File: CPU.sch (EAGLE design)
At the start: 13 parts, among them IC1 Z80CPU, IC4 XR-16C550P, IC5 HM62256DIP, J1 DCJ0202

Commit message: Start Splitting into multiple boards
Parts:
- removed D1: 1N4942, diode:1N4942
- removed IC5: HM62256DIP, jean:HM62256DIP
- removed J1: DCJ0202, con-jack:DCJ0202
- removed U$1: AT28C256ZIF, bt_memory:AT28C256ZIF
- added JP1: (no value), jean:JEANNECTOR/90
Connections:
- removed net !IORQ: IC1.IORQ, V2/3.B, V2/4.A
- removed net !MREQ: IC1.MREQ, V2/1.A, V3/3.B
- removed net N$2: U$1.!CE, V3/3.Y
- removed net N$4: V2/1.B, V3/2.Y
- new net N$1: IC1.M1, JP1.!M1
- new net N$10: IC1.WR, JP1.!WR
- new net N$14: IC1.RD, JP1.!RD
- new net N$16: IC1.IORQ, JP1.!IOREQ
- new net N$19: V2/4.A
- new net N$22: IC1.BUSAK, JP1.!BUSACK
- new net N$8: IC1.MREQ, JP1.!MREQ
- net !RD: no longer IC1.RD, IC5.!RE, U$1.!OE
- net !RESET: now also JP1.!RESET
- net !WR: no longer IC1.WR, IC5.!WE
- net A0: now also JP1.A0; no longer IC5.A0, U$1.A0
- net A1: now also JP1.A1; no longer IC5.A1, U$1.A1
- net A10: now also JP1.A10; no longer IC5.A10, U$1.A10
- net A11: now also JP1.A11; no longer IC5.A11, U$1.A11
- net A12: now also JP1.A12; no longer IC5.A12, U$1.A12
- net A13: now also JP1.A13; no longer IC5.A13, U$1.A13
- net A14: now also JP1.A14; no longer IC5.A14, U$1.A14
- net A15: now also JP1.A15; no longer V3/2.A, V3/2.B, V3/3.A
- net A2: now also JP1.A2; no longer IC5.A2, U$1.A2
- net A3: now also JP1.A3; no longer IC5.A3, U$1.A3
- net A4: now also JP1.A4; no longer IC5.A4, U$1.A4
- net A5: now also JP1.A5; no longer IC5.A5, U$1.A5
- net A6: now also JP1.A6; no longer IC5.A6, U$1.A6
- net A7: now also JP1.A7; no longer IC5.A7, U$1.A7, V2/3.A
- net A8: now also JP1.A8; no longer IC5.A8, U$1.A8
- net A9: now also JP1.A9; no longer IC5.A9, U$1.A9
- net CLOCK: now also JP1.CLK
- net D0: now also JP1.D0; no longer IC5.D0, U$1.IO0
- net D1: now also JP1.D1; no longer IC5.D1, U$1.IO1
- net D2: now also JP1.D2; no longer IC5.D2, U$1.IO2
- net D3: now also JP1.D3; no longer IC5.D3, U$1.IO3
- net D4: now also JP1.D4; no longer IC5.D4, U$1.IO4
- net D5: now also JP1.D5; no longer IC5.D5, U$1.IO5
- net D6: now also JP1.D6; no longer IC5.D6, U$1.IO6
- net D7: now also JP1.D7; no longer IC5.D7, U$1.IO7
- net GND: now also JP1.GND@1, JP1.GND@2; no longer D1.A, IC5.GND, J1.3, U$1.GND
- net N$9: now also IC1.HALT, JP1.!HALT; no longer IC5.!CE, V2/1.Y
- net VCC: now also JP1.!BUSRQ, JP1.!INT, JP1.!NMI, JP1.VCC; no longer D1.C, IC5.VCC, J1.1, U$1.VCC
- net WAIT: now also JP1.!WAIT
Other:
- note removed: "0x0000 - 0x7FFF"
- note removed: "0x8000 - 0xFFFF"

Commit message: Move away Serial CF
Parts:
- removed IC4: XR-16C550P, exar:XR-16C550P
- removed R1: 1k, eagle-ltspice:R0207/10
- removed S1: RESET, switch-omron:10-XX
- removed SV1: SERIAL, con-lstb:MA04-1
- removed SV2: IDE PATA, con-lstb:MA20-2
- removed V2, V3: 74HC00N, 74ttl-din:74HC00N
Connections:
- removed net !RD: IC4G$1.IOR~, SV2.25
- removed net !WR: IC4G$1.IOW~, SV2.23
- removed net IOCS1: SV2.37, V2/4.Y
- removed net N$11: IC4G$1.TX, SV1.1
- removed net N$13: IC4G$1.BAUDOUT~, IC4G$1.RCLK
- removed net N$15: IC4G$1.RX, SV1.2
- removed net N$17: V2/4.B, V3/1.Y
- removed net N$18: IC4G$1.CS2~, V2/3.Y
- removed net N$19: V2/4.A
- removed net N$20: R1.1, SV2.38
- removed net RESET: IC4G$1.RESET, V2/2.Y
- net !RESET: no longer S1.S, S1.S1, SV2.1, V2/2.A, V2/2.B
- net A0: no longer IC4G$1.A0, SV2.35
- net A1: no longer IC4G$1.A1, SV2.33
- net A2: no longer IC4G$1.A2, SV2.36
- net A7: no longer V3/1.A, V3/1.B
- net CLOCK: no longer IC4G$1.XTAL1
- net D0: no longer IC4G$1.D0, SV2.17
- net D1: no longer IC4G$1.D1, SV2.15
- net D2: no longer IC4G$1.D2, SV2.13
- net D3: no longer IC4G$1.D3, SV2.11
- net D4: no longer IC4G$1.D4, SV2.9
- net D5: no longer IC4G$1.D5, SV2.7
- net D6: no longer IC4G$1.D6, SV2.5
- net D7: no longer IC4G$1.D7, SV2.3
- net GND: no longer IC4G$1.AS~, IC4G$1.IOR, IC4G$1.IOW, S1.P, SV1.4, SV2.19, SV2.2, SV2.22, SV2.24, SV2.26, SV2.30, SV2.40, V2/-UB.-UB, V3/-UB.-UB
- net VCC: no longer IC4G$1.CD~, IC4G$1.CS0, IC4G$1.CS1, IC4G$1.DSR~, IC4G$1.RI~, R1.2, SV1.3, SV2.20, V2/+UB.+UB, V3/+UB.+UB
- net WAIT: no longer SV2.27
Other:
- note removed: "A7 = 0"
- note removed: "A7 = 1"

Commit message: Finish Modularization
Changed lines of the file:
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@@
 <wire x1="96.52" y1="20.32" x2="104.14" y2="20.32" width="0.1524" layer="91"/>
 <wire x1="104.14" y1="20.32" x2="104.14" y2="5.08" width="0.1524" layer="91"/>
-<wire x1="104.14" y1="5.08" x2="-10.16" y2="5.08" width="0.1524" layer="91"/>
-<wire x1="-10.16" y1="5.08" x2="-10.16" y2="43.18" width="0.1524" layer="91"/>
+<wire x1="104.14" y1="5.08" x2="-11.684" y2="5.08" width="0.1524" layer="91"/>
+<wire x1="-11.684" y1="5.08" x2="-11.684" y2="43.18" width="0.1524" layer="91"/>
 <pinref part="IC1" gate="1" pin="BUSAK"/>
-<wire x1="-10.16" y1="43.18" x2="-5.08" y2="43.18" width="0.1524" layer="91"/>
+<wire x1="-11.684" y1="43.18" x2="-5.08" y2="43.18" width="0.1524" layer="91"/>
 </segment>
 </net>
@@
 </sheet>
 </sheets>
-<errors>
-</errors>
 </schematic>
 </drawing>

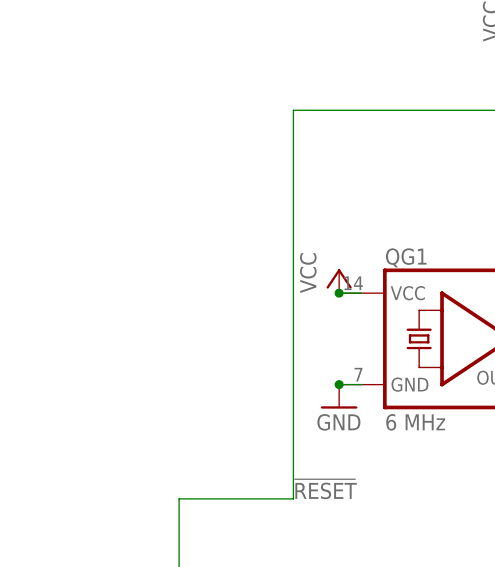
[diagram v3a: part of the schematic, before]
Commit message: Add Decoupling Capacitors.
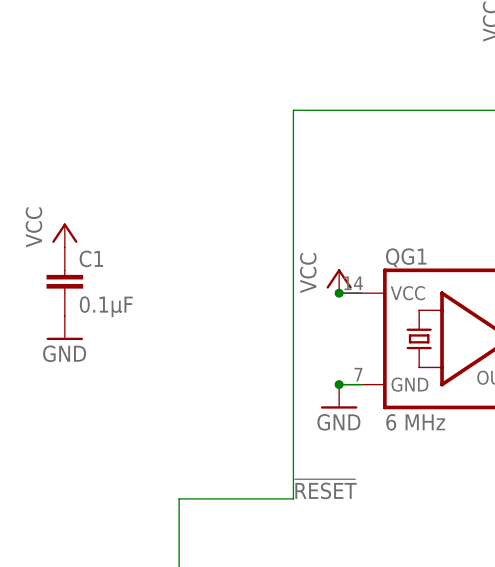
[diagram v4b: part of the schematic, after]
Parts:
- added C1: 0.1µF, capacitor-wima:C5/2.5
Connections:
- net GND: now also C1.2
- net VCC: now also C1.1
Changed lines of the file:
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@@
 <part name="GND1" library="supply1" deviceset="GND" device=""/>
 <part name="GND2" library="supply1" deviceset="GND" device=""/>
+<part name="C1" library="capacitor-wima" deviceset="C" device="5/2.5" value="0.1µF"/>
+<part name="P+1" library="supply1" deviceset="VCC" device=""/>
+<part name="GND3" library="supply1" deviceset="GND" device=""/>
 </parts>
 <sheets>
@@
 <instance part="GND1" gate="1" x="137.16" y="48.26"/>
 <instance part="GND2" gate="1" x="127" y="15.24"/>
+<instance part="C1" gate="G$1" x="-83.82" y="45.72"/>
+<instance part="P+1" gate="VCC" x="-83.82" y="50.8"/>
+<instance part="GND3" gate="1" x="-83.82" y="38.1"/>
 </instances>
 <busses>
@@
 <wire x1="96.52" y1="53.34" x2="137.16" y2="53.34" width="0.1524" layer="91"/>
 </segment>
+<segment>
+<pinref part="C1" gate="G$1" pin="1"/>
+<pinref part="P+1" gate="VCC" pin="VCC"/>
+</segment>
 </net>
 <net name="GND" class="0">
@@
 <wire x1="129.54" y1="55.88" x2="96.52" y2="55.88" width="0.1524" layer="91"/>
 </segment>
-</net>
+<segment>
+<pinref part="C1" gate="G$1" pin="2"/>
+<pinref part="GND3" gate="1" pin="GND"/>
+</segment>
+</net>

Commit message: Add PullUp to reset of cpu
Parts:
- added R1: 3.3k, resistor:R-EU_0207/2V
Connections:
- net !RESET: now also R1.1
- net VCC: now also R1.2
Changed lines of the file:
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@@
 <part name="P+1" library="supply1" deviceset="VCC" device=""/>
 <part name="GND3" library="supply1" deviceset="GND" device=""/>
+<part name="R1" library="resistor" deviceset="R-EU_" device="0207/2V" value="3.3k"/>
+<part name="P+3" library="supply1" deviceset="VCC" device=""/>
 </parts>
 <sheets>
@@
 <instance part="P+1" gate="VCC" x="-83.82" y="50.8"/>
 <instance part="GND3" gate="1" x="-83.82" y="38.1"/>
+<instance part="R1" gate="G$1" x="-53.34" y="68.58" rot="R90"/>
+<instance part="P+3" gate="VCC" x="-53.34" y="76.2"/>
 </instances>
 <busses>
@@
 <pinref part="P+1" gate="VCC" pin="VCC"/>
 </segment>
+<segment>
+<pinref part="R1" gate="G$1" pin="2"/>
+<pinref part="P+3" gate="VCC" pin="VCC"/>
+</segment>
 </net>
 <net name="GND" class="0">
@@
 <wire x1="-71.12" y1="-20.32" x2="-71.12" y2="20.32" width="0.1524" layer="91"/>
 <wire x1="-71.12" y1="20.32" x2="-58.42" y2="20.32" width="0.1524" layer="91"/>
-<wire x1="-10.16" y1="63.5" x2="-58.42" y2="63.5" width="0.1524" layer="91"/>
-</segment>
-</net>
+<wire x1="-10.16" y1="63.5" x2="-53.34" y2="63.5" width="0.1524" layer="91"/>
+<pinref part="R1" gate="G$1" pin="1"/>
+<wire x1="-53.34" y1="63.5" x2="-58.42" y2="63.5" width="0.1524" layer="91"/>
+<junction x="-53.34" y="63.5"/>
+</segment>
+</net>

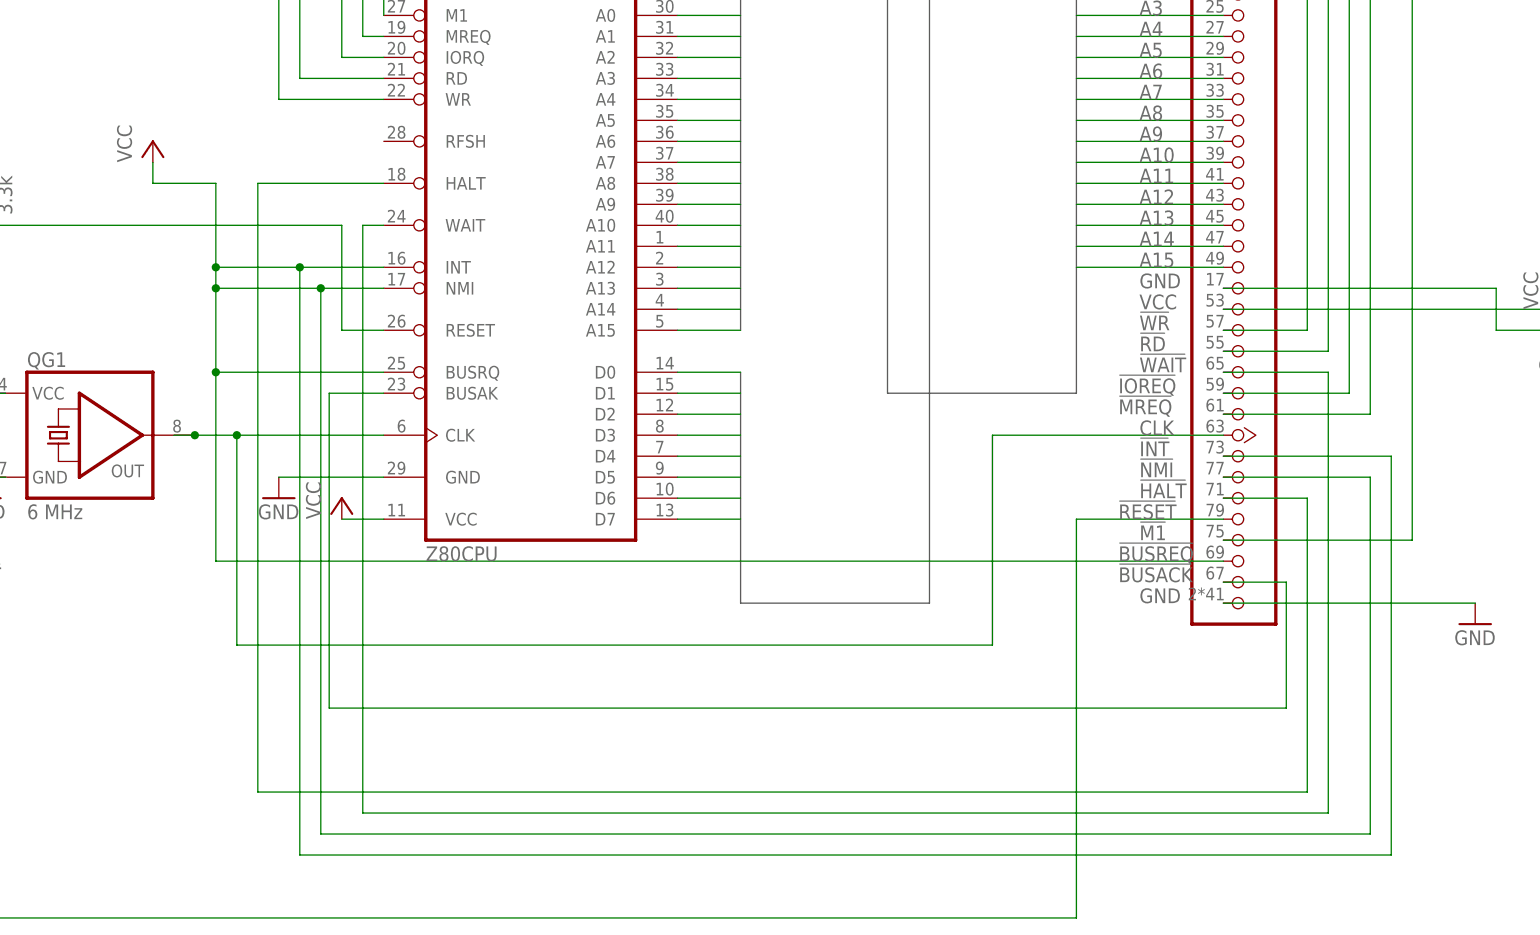
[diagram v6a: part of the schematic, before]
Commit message: Add PullUps to CPU Board
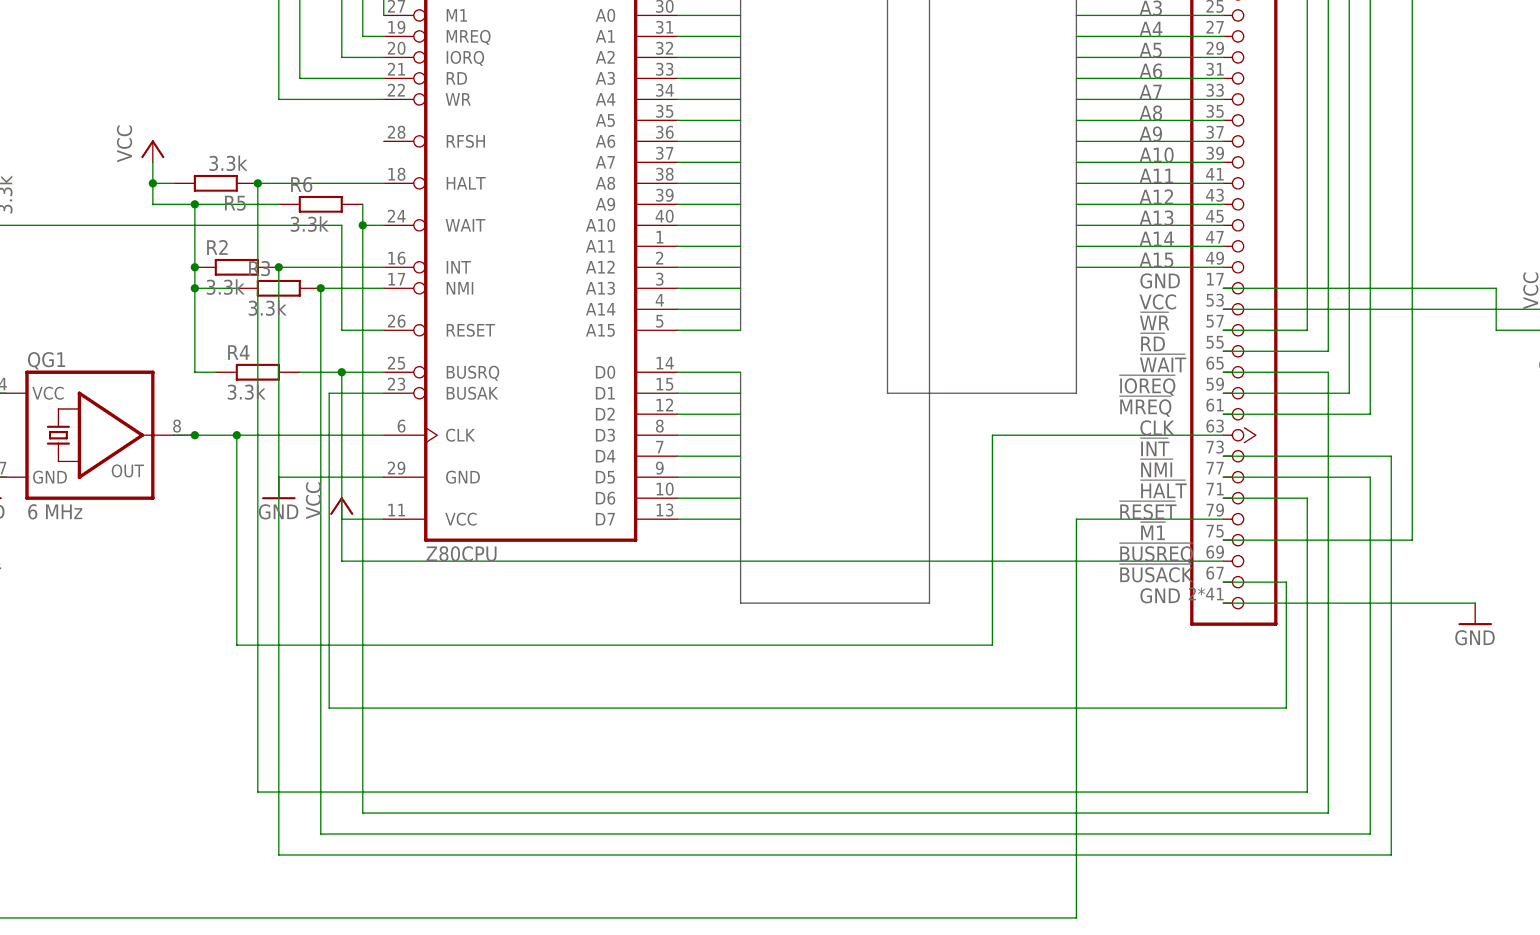
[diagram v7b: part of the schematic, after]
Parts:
- added R2, R3, R4, R5, R6: 3.3k, resistor:R-EU_0207/2V
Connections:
- new net N$2: IC1.BUSRQ, JP1.!BUSRQ, R4.2
- new net N$3: IC1.NMI, JP1.!NMI, R3.2
- new net N$4: IC1.INT, JP1.!INT, R2.2
- net N$9: now also R5.1
- net VCC: now also R2.1, R3.1, R4.1, R5.2, R6.1; no longer IC1.BUSRQ, IC1.INT, IC1.NMI, JP1.!BUSRQ, JP1.!INT, JP1.!NMI
- net WAIT: now also R6.2
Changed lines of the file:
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@@
 <part name="R1" library="resistor" deviceset="R-EU_" device="0207/2V" value="3.3k"/>
 <part name="P+3" library="supply1" deviceset="VCC" device=""/>
+<part name="R2" library="resistor" deviceset="R-EU_" device="0207/2V" value="3.3k"/>
+<part name="R3" library="resistor" deviceset="R-EU_" device="0207/2V" value="3.3k"/>
+<part name="R4" library="resistor" deviceset="R-EU_" device="0207/2V" value="3.3k"/>
+<part name="R5" library="resistor" deviceset="R-EU_" device="0207/2V" value="3.3k"/>
+<part name="R6" library="resistor" deviceset="R-EU_" device="0207/2V" value="3.3k"/>
 </parts>
 <sheets>
@@
 <instance part="R1" gate="G$1" x="-53.34" y="68.58" rot="R90"/>
 <instance part="P+3" gate="VCC" x="-53.34" y="76.2"/>
+<instance part="R2" gate="G$1" x="-22.86" y="58.42"/>
+<instance part="R3" gate="G$1" x="-17.78" y="55.88"/>
+<instance part="R4" gate="G$1" x="-20.32" y="45.72"/>
+<instance part="R5" gate="G$1" x="-25.4" y="68.58" rot="R180"/>
+<instance part="R6" gate="G$1" x="-12.7" y="66.04"/>
 </instances>
 <busses>
@@
 <pinref part="P+10" gate="VCC" pin="VCC"/>
 <wire x1="-33.02" y1="71.12" x2="-33.02" y2="68.58" width="0.1524" layer="91"/>
-<pinref part="IC1" gate="1" pin="BUSRQ"/>
-<wire x1="-5.08" y1="45.72" x2="-25.4" y2="45.72" width="0.1524" layer="91"/>
-<wire x1="-25.4" y1="45.72" x2="-25.4" y2="55.88" width="0.1524" layer="91"/>
-<wire x1="-25.4" y1="55.88" x2="-25.4" y2="58.42" width="0.1524" layer="91"/>
-<wire x1="-25.4" y1="58.42" x2="-25.4" y2="68.58" width="0.1524" layer="91"/>
-<pinref part="IC1" gate="1" pin="INT"/>
-<wire x1="-5.08" y1="58.42" x2="-15.24" y2="58.42" width="0.1524" layer="91"/>
-<junction x="-25.4" y="58.42"/>
-<pinref part="IC1" gate="1" pin="NMI"/>
-<wire x1="-15.24" y1="58.42" x2="-25.4" y2="58.42" width="0.1524" layer="91"/>
-<wire x1="-5.08" y1="55.88" x2="-12.7" y2="55.88" width="0.1524" layer="91"/>
-<junction x="-25.4" y="55.88"/>
-<wire x1="-12.7" y1="55.88" x2="-25.4" y2="55.88" width="0.1524" layer="91"/>
-<wire x1="-33.02" y1="68.58" x2="-25.4" y2="68.58" width="0.1524" layer="91"/>
-<pinref part="JP1" gate="A" pin="!INT"/>
-<wire x1="96.52" y1="35.56" x2="116.84" y2="35.56" width="0.1524" layer="91"/>
-<wire x1="116.84" y1="35.56" x2="116.84" y2="-12.7" width="0.1524" layer="91"/>
-<wire x1="116.84" y1="-12.7" x2="-15.24" y2="-12.7" width="0.1524" layer="91"/>
-<wire x1="-15.24" y1="-12.7" x2="-15.24" y2="58.42" width="0.1524" layer="91"/>
-<junction x="-15.24" y="58.42"/>
-<wire x1="-12.7" y1="55.88" x2="-12.7" y2="-10.16" width="0.1524" layer="91"/>
-<junction x="-12.7" y="55.88"/>
-<wire x1="-12.7" y1="-10.16" x2="114.3" y2="-10.16" width="0.1524" layer="91"/>
-<wire x1="114.3" y1="-10.16" x2="114.3" y2="33.02" width="0.1524" layer="91"/>
-<pinref part="JP1" gate="A" pin="!NMI"/>
-<wire x1="114.3" y1="33.02" x2="96.52" y2="33.02" width="0.1524" layer="91"/>
-<pinref part="JP1" gate="A" pin="!BUSRQ"/>
-<wire x1="96.52" y1="22.86" x2="-25.4" y2="22.86" width="0.1524" layer="91"/>
-<wire x1="-25.4" y1="22.86" x2="-25.4" y2="45.72" width="0.1524" layer="91"/>
-<junction x="-25.4" y="45.72"/>
+<wire x1="-33.02" y1="68.58" x2="-33.02" y2="66.04" width="0.1524" layer="91"/>
+<wire x1="-27.94" y1="45.72" x2="-27.94" y2="55.88" width="0.1524" layer="91"/>
+<pinref part="R2" gate="G$1" pin="1"/>
+<wire x1="-27.94" y1="55.88" x2="-27.94" y2="58.42" width="0.1524" layer="91"/>
+<wire x1="-27.94" y1="58.42" x2="-27.94" y2="66.04" width="0.1524" layer="91"/>
+<junction x="-27.94" y="58.42"/>
+<pinref part="R3" gate="G$1" pin="1"/>
+<wire x1="-22.86" y1="55.88" x2="-27.94" y2="55.88" width="0.1524" layer="91"/>
+<junction x="-27.94" y="55.88"/>
+<pinref part="R4" gate="G$1" pin="1"/>
+<wire x1="-27.94" y1="45.72" x2="-25.4" y2="45.72" width="0.1524" layer="91"/>
+<pinref part="R6" gate="G$1" pin="1"/>
+<wire x1="-17.78" y1="66.04" x2="-27.94" y2="66.04" width="0.1524" layer="91"/>
+<wire x1="-33.02" y1="66.04" x2="-27.94" y2="66.04" width="0.1524" layer="91"/>
+<junction x="-27.94" y="66.04"/>
+<pinref part="R5" gate="G$1" pin="2"/>
+<wire x1="-33.02" y1="68.58" x2="-30.48" y2="68.58" width="0.1524" layer="91"/>
+<junction x="-33.02" y="68.58"/>
 </segment>
 <segment>
@@
 <wire x1="96.52" y1="45.72" x2="109.22" y2="45.72" width="0.1524" layer="91"/>
 <wire x1="109.22" y1="45.72" x2="109.22" y2="-7.62" width="0.1524" layer="91"/>
+<pinref part="R6" gate="G$1" pin="2"/>
+<wire x1="-7.62" y1="66.04" x2="-7.62" y2="63.5" width="0.1524" layer="91"/>
+<junction x="-7.62" y="63.5"/>
 </segment>
 </net>
@@
 <wire x1="106.68" y1="30.48" x2="106.68" y2="-5.08" width="0.1524" layer="91"/>
 <wire x1="106.68" y1="-5.08" x2="-20.32" y2="-5.08" width="0.1524" layer="91"/>
-<wire x1="-20.32" y1="-5.08" x2="-20.32" y2="68.58" width="0.1524" layer="91"/>
+<pinref part="R5" gate="G$1" pin="1"/>
 <pinref part="IC1" gate="1" pin="HALT"/>
 <wire x1="-20.32" y1="68.58" x2="-5.08" y2="68.58" width="0.1524" layer="91"/>
+<wire x1="-20.32" y1="-5.08" x2="-20.32" y2="68.58" width="0.1524" layer="91"/>
+<junction x="-20.32" y="68.58"/>
 </segment>
 </net>
@@
 </segment>
 </net>
+<net name="N$2" class="0">
+<segment>
+<pinref part="JP1" gate="A" pin="!BUSRQ"/>
+<wire x1="96.52" y1="22.86" x2="-10.16" y2="22.86" width="0.1524" layer="91"/>
+<pinref part="IC1" gate="1" pin="BUSRQ"/>
+<wire x1="-5.08" y1="45.72" x2="-10.16" y2="45.72" width="0.1524" layer="91"/>
+<wire x1="-10.16" y1="45.72" x2="-10.16" y2="22.86" width="0.1524" layer="91"/>
+<pinref part="R4" gate="G$1" pin="2"/>
+<wire x1="-10.16" y1="45.72" x2="-15.24" y2="45.72" width="0.1524" layer="91"/>
+<junction x="-10.16" y="45.72"/>
+</segment>
+</net>
+<net name="N$3" class="0">
+<segment>
+<pinref part="JP1" gate="A" pin="!NMI"/>
+<wire x1="114.3" y1="33.02" x2="96.52" y2="33.02" width="0.1524" layer="91"/>
+<wire x1="114.3" y1="-10.16" x2="114.3" y2="33.02" width="0.1524" layer="91"/>
+<pinref part="IC1" gate="1" pin="NMI"/>
+<wire x1="-5.08" y1="55.88" x2="-12.7" y2="55.88" width="0.1524" layer="91"/>
+<wire x1="-12.7" y1="55.88" x2="-12.7" y2="-10.16" width="0.1524" layer="91"/>
+<wire x1="-12.7" y1="-10.16" x2="114.3" y2="-10.16" width="0.1524" layer="91"/>
+<pinref part="R3" gate="G$1" pin="2"/>
+<junction x="-12.7" y="55.88"/>
+</segment>
+</net>
+<net name="N$4" class="0">
+<segment>
+<pinref part="IC1" gate="1" pin="INT"/>
+<wire x1="-5.08" y1="58.42" x2="-17.78" y2="58.42" width="0.1524" layer="91"/>
+<pinref part="JP1" gate="A" pin="!INT"/>
+<wire x1="96.52" y1="35.56" x2="116.84" y2="35.56" width="0.1524" layer="91"/>
+<wire x1="116.84" y1="35.56" x2="116.84" y2="-12.7" width="0.1524" layer="91"/>
+<wire x1="116.84" y1="-12.7" x2="-17.78" y2="-12.7" width="0.1524" layer="91"/>
+<wire x1="-17.78" y1="-12.7" x2="-17.78" y2="58.42" width="0.1524" layer="91"/>
+<pinref part="R2" gate="G$1" pin="2"/>
+<junction x="-17.78" y="58.42"/>
+</segment>
+</net>
